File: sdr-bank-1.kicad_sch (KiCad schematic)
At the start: 32 parts, among them U1 IS42S86400F-7TL, U2 IS42S86400F-7TL, U3 IS42S86400F-7TL, U4 IS42S86400F-7TL

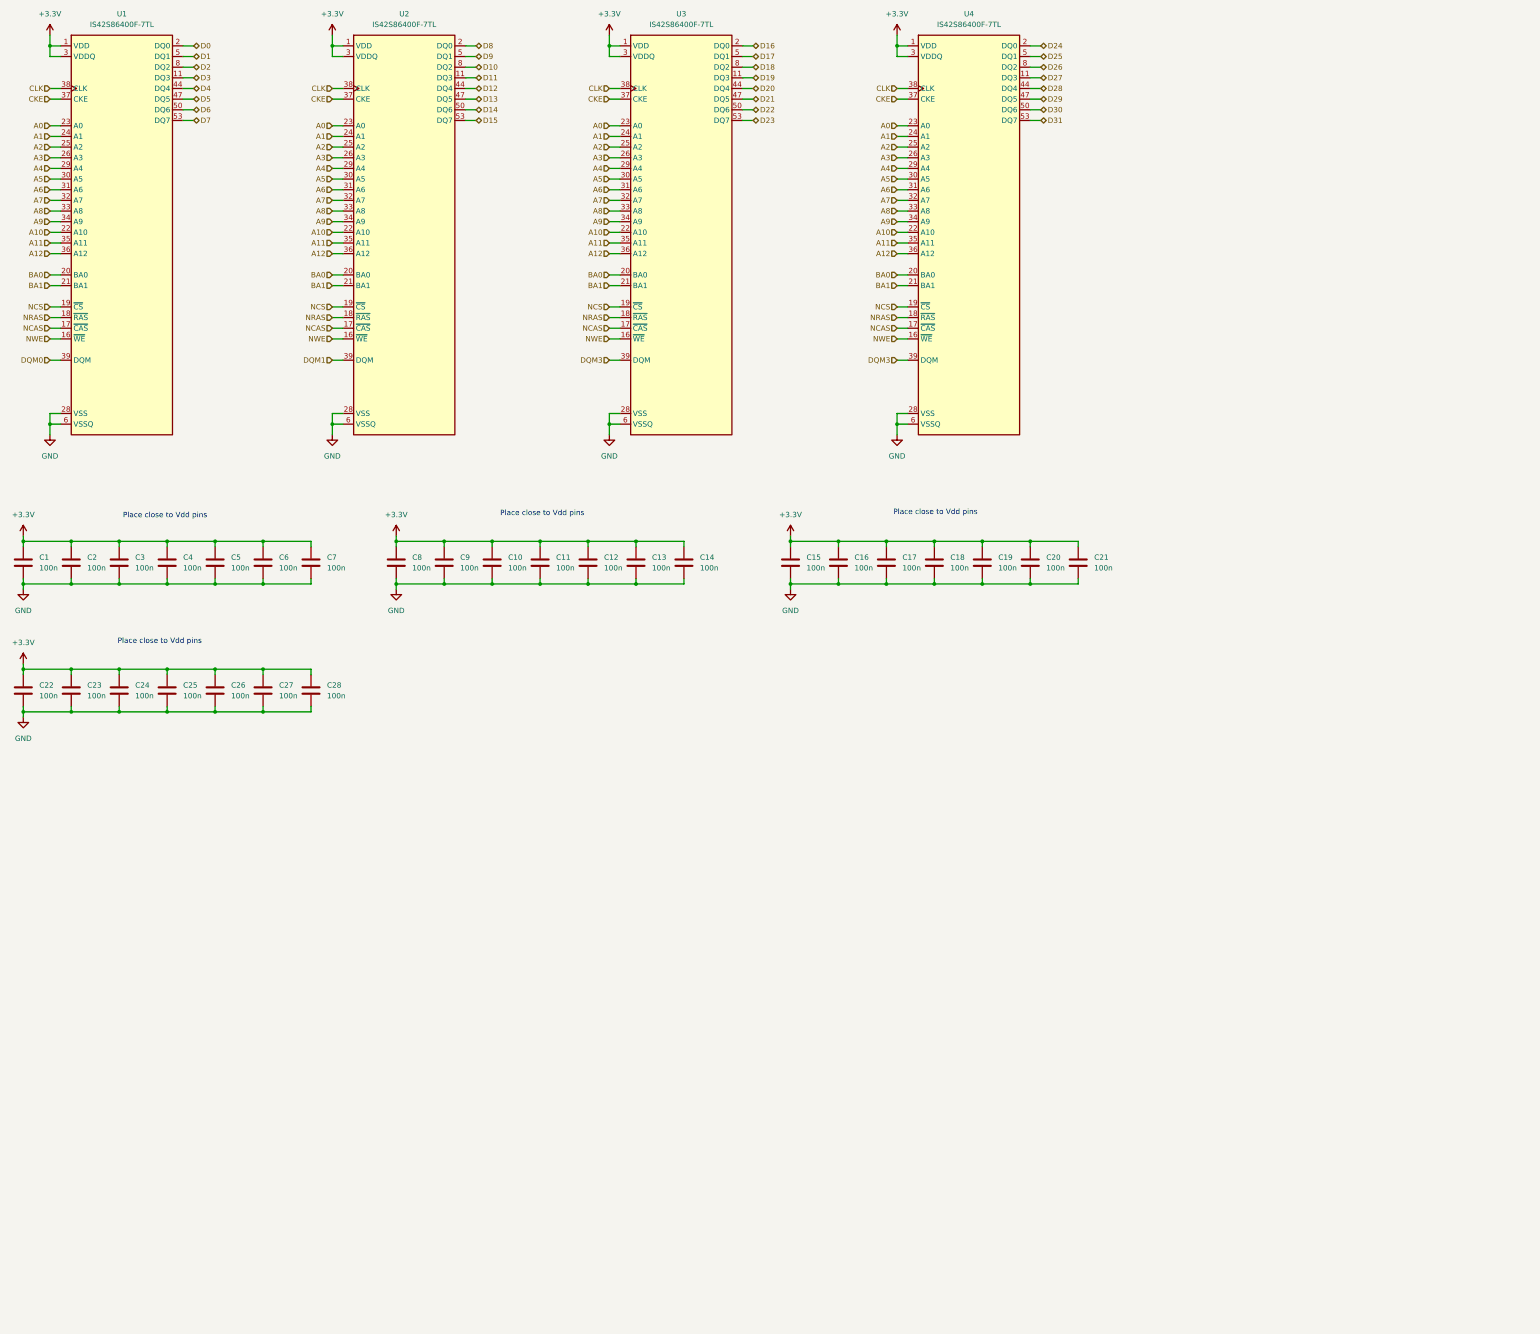
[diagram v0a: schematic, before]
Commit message: [#100470] Connect SODIMM to SDRAM banks
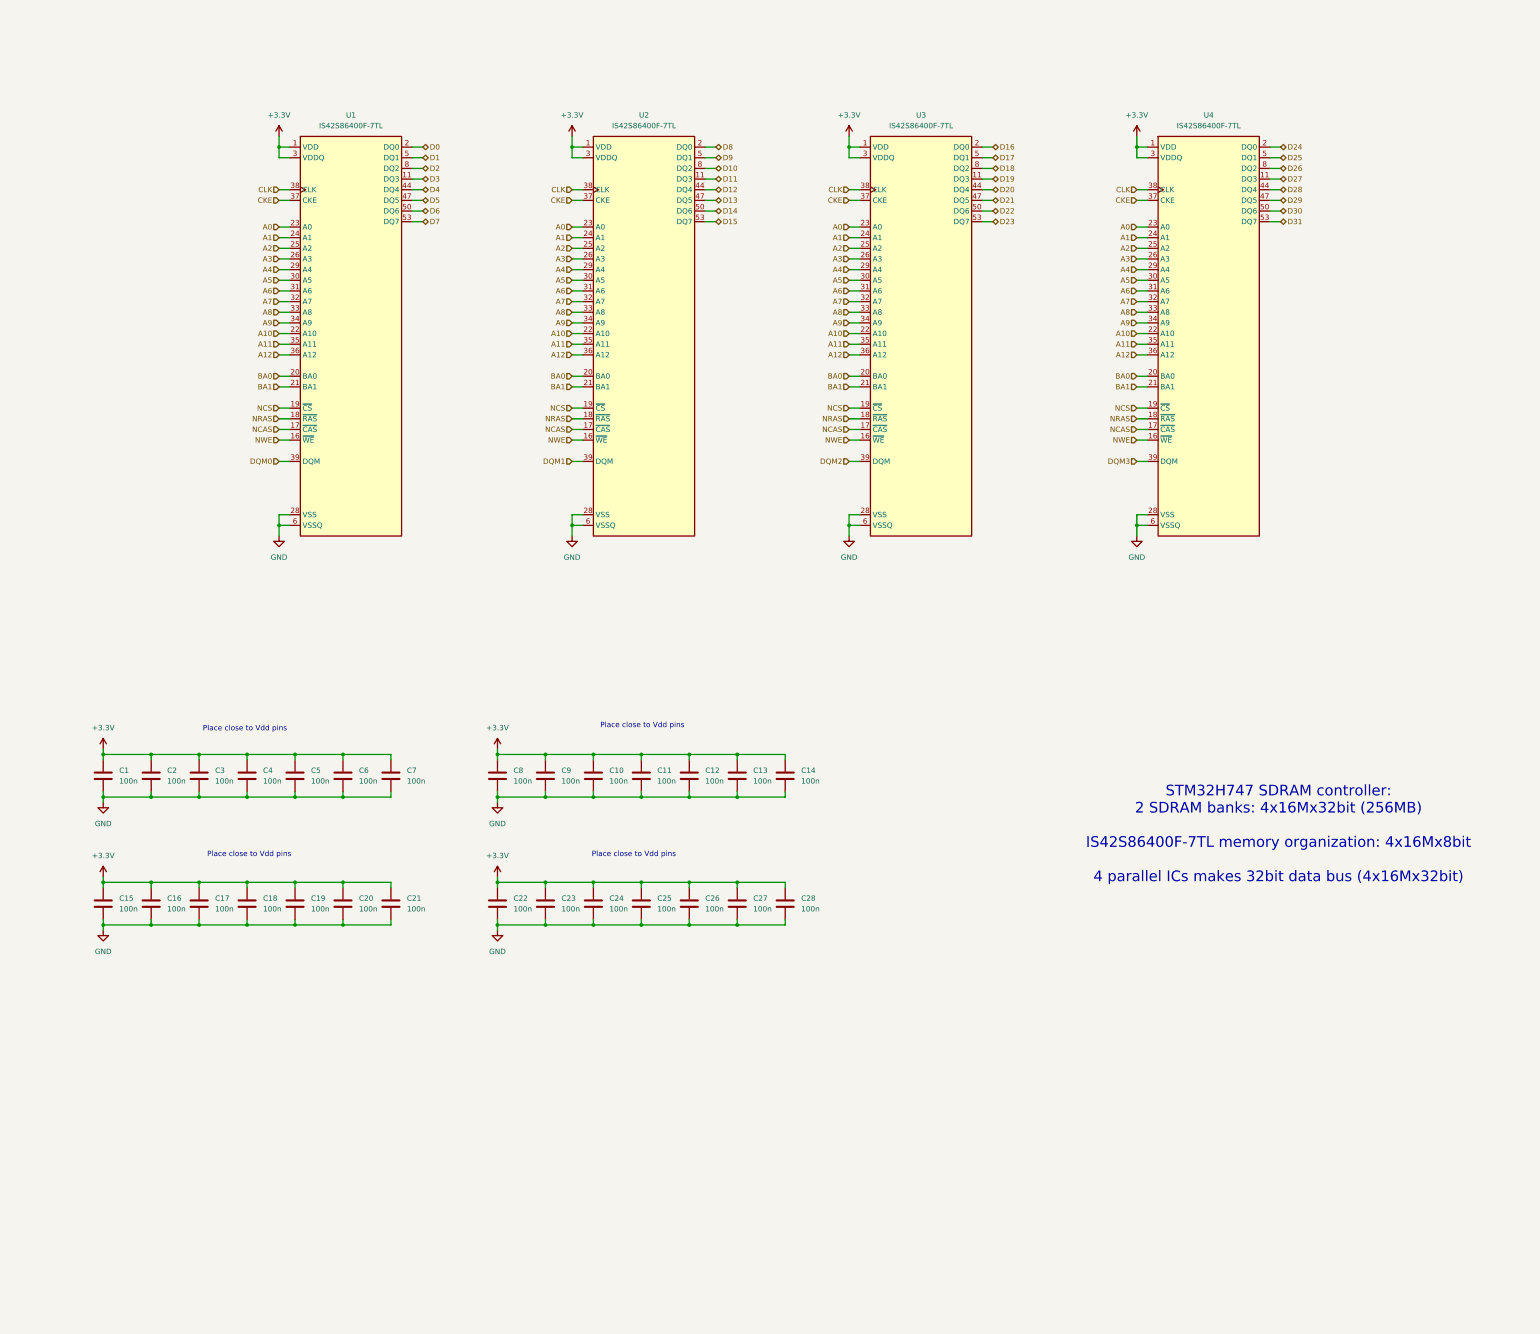
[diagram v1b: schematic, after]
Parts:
- renumbered C17 to C10, C18 to C11, C19 to C12, C20 to C13, C21 to C14, C8 to C15, C9 to C16, C10 to C17, C11 to C18, C12 to C19, C13 to C20, C14 to C21, C15 to C8, C16 to C9
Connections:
- net DQM3: no longer U3.39 (DQM)
- new net DQM2: U3.39 (DQM)
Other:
- note added: "STM32H747 SDRAM controller: 2 SDRAM banks: 4x16Mx32bit (256MB) IS42S86400F-7TL memory organization: 4x16Mx8bit 4 parallel ICs makes 32bit data bus (4x16Mx32bit)"
- company: (none) -> Antmicro Ltd
- title: (none) -> STM32H7 HDMI Board SODIMM
- moved on the sheet: C1, C10, C11, C12, C13, C14, C15, C16, C17, C18, C19, C2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

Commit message: [#100470] Add 1u decoupling capacitors to schematic
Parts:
- added C16, C24, C32, C8: 1u, symbol Device:C
- renumbered C9 to C10, C10 to C11, C11 to C12, C12 to C13, C13 to C14, C14 to C15, C15 to C17, C16 to C18, C17 to C19, C18 to C20, C19 to C21, C20 to C22, C21 to C23, C22 to C25, C23 to C26, C24 to C27, C25 to C28, C26 to C29, C27 to C30, C28 to C31, C8 to C9
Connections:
- net +3.3V: now also C16.1, C24.1, C32.1, C8.1
- net GND: now also C16.2, C24.2, C32.2, C8.2
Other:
- moved on the sheet: C10, C11, C12, C13, C14, C15, C25, C26, C27, C28, C29, C30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

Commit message: [#100470] Switch to R in packs, assign footprints
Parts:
- C1, C10, C11, C12, C13, C14, C15, C16, C17, C18, C19, C2, C20, C21, C22, C23, C24, C25, C26, C27, C28, C29, C3, C30, C31, C32, C4, C5, C6, C7, C8, C9: footprint (none) -> antmicro-footprints:C_0402_1005Metric
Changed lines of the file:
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@@
 			)
 		)
-		(property "Footprint" ""
+		(property "Footprint" "antmicro-footprints:C_0402_1005Metric"
 			(at 234.6452 236.22 0)
 			(hide yes)
@@
 			)
 		)
-		(property "Footprint" ""
+		(property "Footprint" "antmicro-footprints:C_0402_1005Metric"
 			(at 55.5752 205.74 0)
 			(hide yes)
@@
 			)
 		)
-		(property "Footprint" ""
+		(property "Footprint" "antmicro-footprints:C_0402_1005Metric"
 			(at 223.2152 205.74 0)
 			(hide yes)
@@
 			)
 		)
-		(property "Footprint" ""
+		(property "Footprint" "antmicro-footprints:C_0402_1005Metric"
 			(at 177.4952 236.22 0)
 			(hide yes)
@@
 			)
 		)
-		(property "Footprint" ""
+		(property "Footprint" "antmicro-footprints:C_0402_1005Metric"
 			(at 200.3552 205.74 0)
 			(hide yes)
@@
 			)
 		)
-		(property "Footprint" ""
+		(property "Footprint" "antmicro-footprints:C_0402_1005Metric"
 			(at 101.2952 236.22 0)
 			(hide yes)
@@
 			)
 		)
-		(property "Footprint" ""
+		(property "Footprint" "antmicro-footprints:C_0402_1005Metric"
 			(at 78.4352 205.74 0)
 			(hide yes)
@@
 			)
 		)
-		(property "Footprint" ""
+		(property "Footprint" "antmicro-footprints:C_0402_1005Metric"
 			(at 154.6352 236.22 0)
 			(hide yes)
@@
 			)
 		)
-		(property "Footprint" ""
+		(property "Footprint" "antmicro-footprints:C_0402_1005Metric"
 			(at 154.6352 205.74 0)
 			(hide yes)
@@
 			)
 		)
-		(property "Footprint" ""
+		(property "Footprint" "antmicro-footprints:C_0402_1005Metric"
 			(at 234.6452 205.74 0)
 			(hide yes)
@@
 			)
 		)
-		(property "Footprint" ""
+		(property "Footprint" "antmicro-footprints:C_0402_1005Metric"
 			(at 211.7852 236.22 0)
 			(hide yes)
@@
 			)
 		)
-		(property "Footprint" ""
+		(property "Footprint" "antmicro-footprints:C_0402_1005Metric"
 			(at 44.1452 205.74 0)
 			(hide yes)
@@
 			)
 		)
-		(property "Footprint" ""
+		(property "Footprint" "antmicro-footprints:C_0402_1005Metric"
 			(at 101.2952 205.74 0)
 			(hide yes)
@@
 			)
 		)
-		(property "Footprint" ""
+		(property "Footprint" "antmicro-footprints:C_0402_1005Metric"
 			(at 67.0052 205.74 0)
 			(hide yes)
@@
 			)
 		)
-		(property "Footprint" ""
+		(property "Footprint" "antmicro-footprints:C_0402_1005Metric"
 			(at 89.8652 236.22 0)
 			(hide yes)
@@
 			)
 		)
-		(property "Footprint" ""
+		(property "Footprint" "antmicro-footprints:C_0402_1005Metric"
 			(at 112.7252 236.22 0)
 			(hide yes)
@@
 			)
 		)
-		(property "Footprint" ""
+		(property "Footprint" "antmicro-footprints:C_0402_1005Metric"
 			(at 223.2152 236.22 0)
 			(hide yes)
@@
 			)
 		)
-		(property "Footprint" ""
+		(property "Footprint" "antmicro-footprints:C_0402_1005Metric"
 			(at 89.8652 205.74 0)
 			(hide yes)
@@
 			)
 		)
-		(property "Footprint" ""
+		(property "Footprint" "antmicro-footprints:C_0402_1005Metric"
 			(at 211.7852 205.74 0)
 			(hide yes)
@@
 			)
 		)
-		(property "Footprint" ""
+		(property "Footprint" "antmicro-footprints:C_0402_1005Metric"
 			(at 44.1452 236.22 0)
 			(hide yes)
@@
 			)
 		)
-		(property "Footprint" ""
+		(property "Footprint" "antmicro-footprints:C_0402_1005Metric"
 			(at 67.0052 236.22 0)
 			(hide yes)
@@
 			)
 		)
-		(property "Footprint" ""
+		(property "Footprint" "antmicro-footprints:C_0402_1005Metric"
 			(at 166.0652 236.22 0)
 			(hide yes)
@@
 			)
 		)
-		(property "Footprint" ""
+		(property "Footprint" "antmicro-footprints:C_0402_1005Metric"
 			(at 124.1552 236.22 0)
 			(hide yes)
@@
 			)
 		)
-		(property "Footprint" ""
+		(property "Footprint" "antmicro-footprints:C_0402_1005Metric"
 			(at 188.9252 236.22 0)
 			(hide yes)
@@
 			)
 		)
-		(property "Footprint" ""
+		(property "Footprint" "antmicro-footprints:C_0402_1005Metric"
 			(at 112.7252 205.74 0)
 			(hide yes)
@@
 			)
 		)
-		(property "Footprint" ""
+		(property "Footprint" "antmicro-footprints:C_0402_1005Metric"
 			(at 124.1552 205.74 0)
 			(hide yes)
@@
 			)
 		)
-		(property "Footprint" ""
+		(property "Footprint" "antmicro-footprints:C_0402_1005Metric"
 			(at 200.3552 236.22 0)
 			(hide yes)
@@
 			)
 		)
-		(property "Footprint" ""
+		(property "Footprint" "antmicro-footprints:C_0402_1005Metric"
 			(at 177.4952 205.74 0)
 			(hide yes)
@@
 			)
 		)
-		(property "Footprint" ""
+		(property "Footprint" "antmicro-footprints:C_0402_1005Metric"
 			(at 55.5752 236.22 0)
 			(hide yes)
@@
 			)
 		)
-		(property "Footprint" ""
+		(property "Footprint" "antmicro-footprints:C_0402_1005Metric"
 			(at 166.0652 205.74 0)
 			(hide yes)
@@
 			)
 		)
-		(property "Footprint" ""
+		(property "Footprint" "antmicro-footprints:C_0402_1005Metric"
 			(at 78.4352 236.22 0)
 			(hide yes)
@@
 			)
 		)
-		(property "Footprint" ""
+		(property "Footprint" "antmicro-footprints:C_0402_1005Metric"
 			(at 188.9252 205.74 0)
 			(hide yes)
